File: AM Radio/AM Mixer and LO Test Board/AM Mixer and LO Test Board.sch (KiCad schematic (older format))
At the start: 53 parts, among them J1 RF_IN, J2 IF_FILT_OUT, J3 IF_PREFILT_OUT, J4 RF_IN, J5 +12V Input, J6 -12V Input, Q1 2N2222, Q2 2N2222, Q3 2N2222, T1 SWB2010-1-SM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

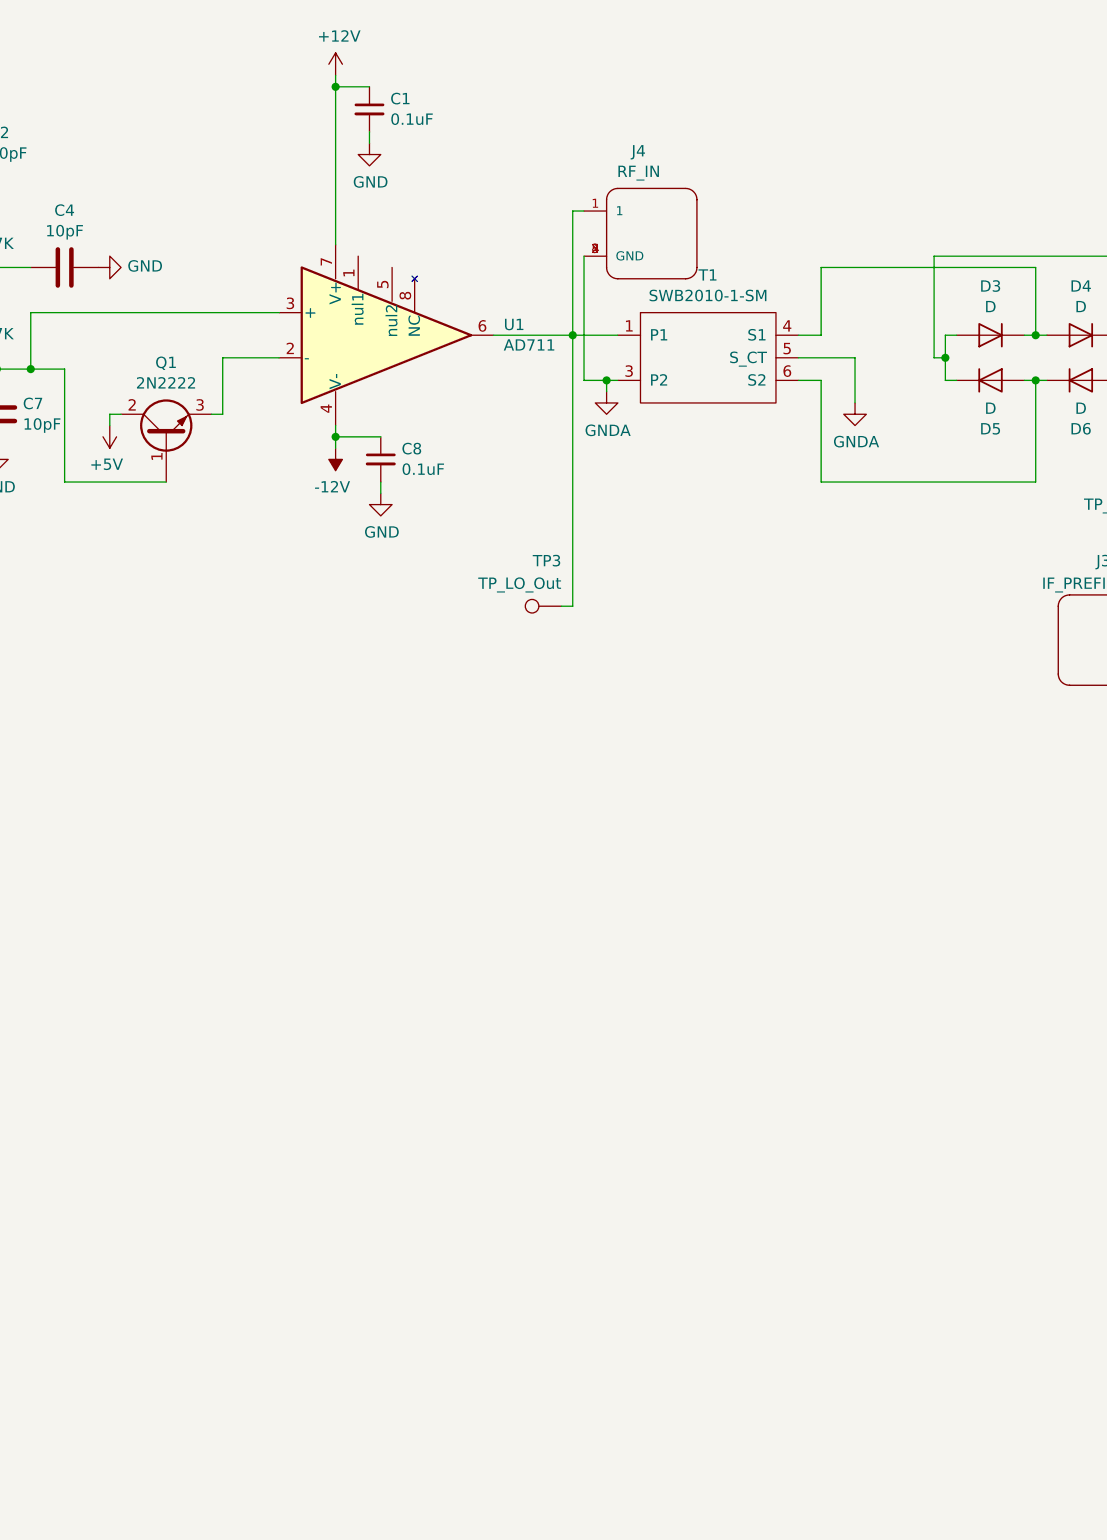
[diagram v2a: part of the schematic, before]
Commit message: Added extra filter for testing. Finished silk screen editing.
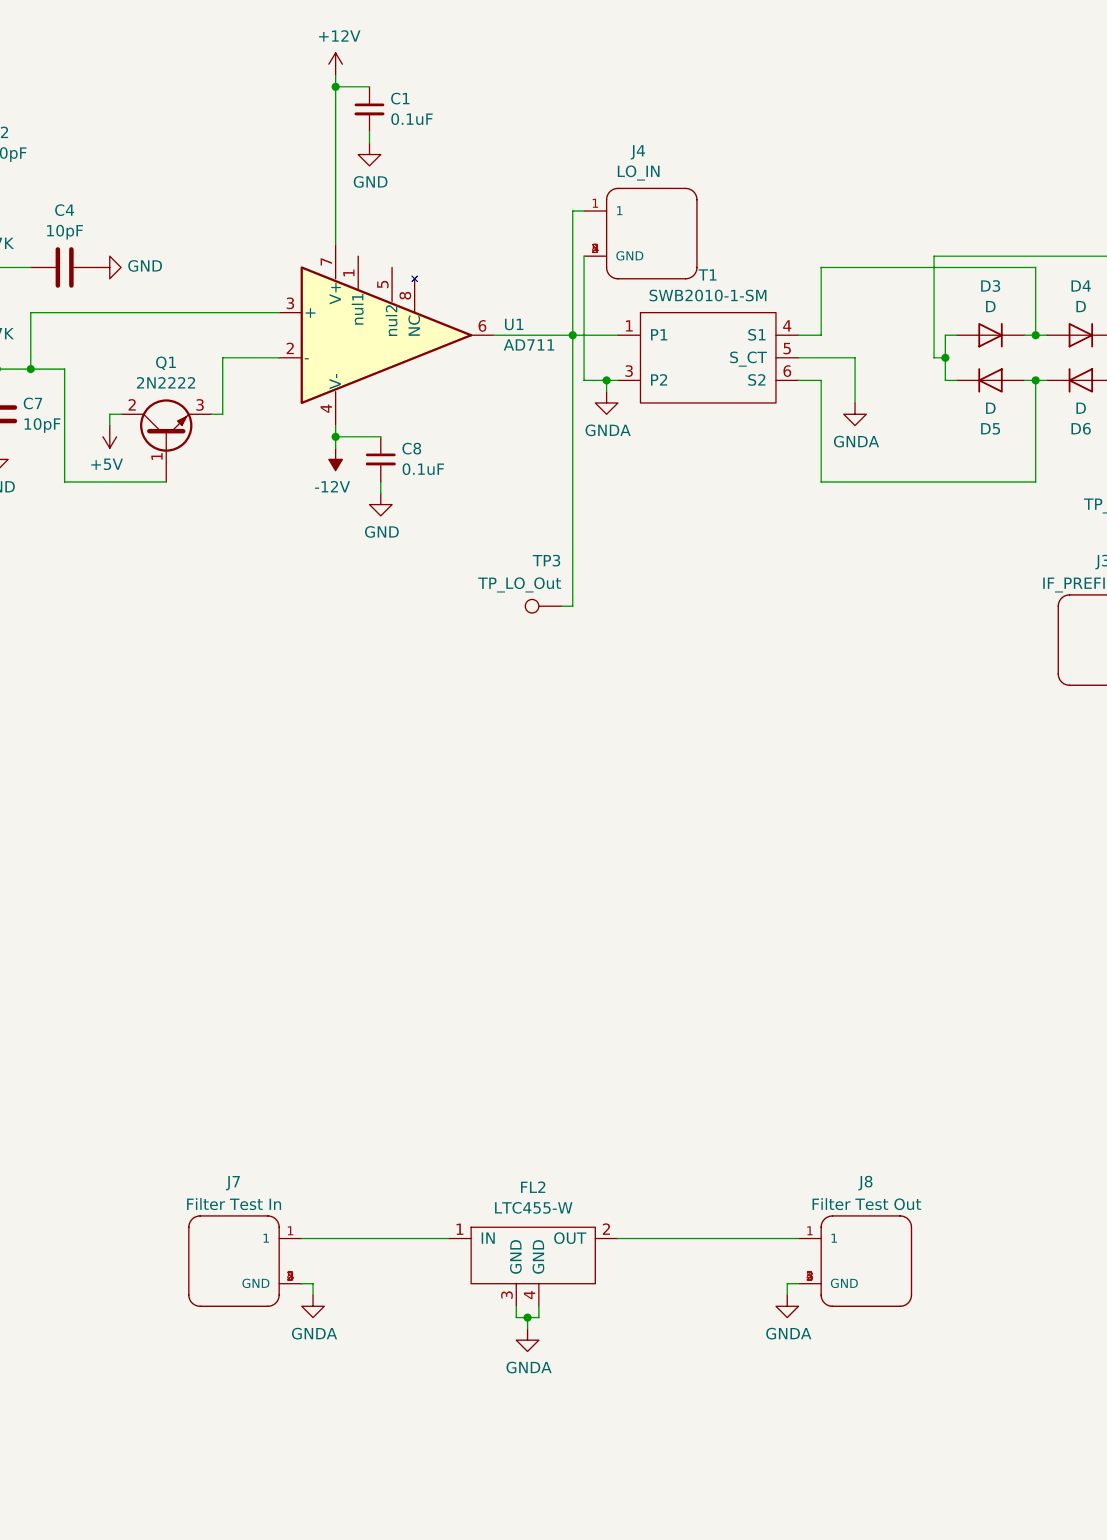
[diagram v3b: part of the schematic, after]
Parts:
- added FL2: LTC455-W, footprints:LTC455-W, symbol CustomComponents:LTC455-W
- added J7: Filter Test In, footprints:TE_5-1634503-1, symbol TE_5-1634503-1:5-1634503-1
- added J8: Filter Test Out, footprints:TE_5-1634503-1, symbol TE_5-1634503-1:5-1634503-1
- J4: value RF_IN -> LO_IN
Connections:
- net GNDA: now also FL2.3 (GND), FL2.4 (GND), J7.2 (GND), J7.3 (GND), J7.4 (GND), J7.5 (GND), J8.2 (GND), J8.3 (GND), J8.4 (GND), J8.5 (GND)
- new net: FL2.2 (OUT), J8.1
- new net: FL2.1 (IN), J7.1
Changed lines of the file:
@@
 P 9900 2750
 F 0 "J4" H 9958 3115 50  0000 C CNN
-F 1 "RF_IN" H 9958 3024 50  0000 C CNN
+F 1 "LO_IN" H 9958 3024 50  0000 C CNN
 F 2 "footprints:TE_5-1634503-1" H 9900 2750 50  0001 L BNN
 F 3 "" H 9900 2750 50  0001 L BNN
@@
 Wire Wire Line
 	4550 1500 4550 1400
+$Comp
+L TE_5-1634503-1:5-1634503-1 J8
+U 1 1 60DEE717
+P 10850 7300
+F 0 "J8" H 10850 7650 50  0000 C CNN
+F 1 "Filter Test Out" H 10850 7550 50  0000 C CNN
+F 2 "footprints:TE_5-1634503-1" H 10850 7300 50  0001 L BNN
+F 3 "" H 10850 7300 50  0001 L BNN
+F 4 "1" H 10850 7300 50  0001 L BNN "Number_of_Positions"
+F 5 "Compliant" H 10850 7300 50  0001 L BNN "EU_RoHS_Compliance"
+F 6 "5-1634503-1" H 10850 7300 50  0001 L BNN "Comment"
+	1    10850 7300
+	-1   0    0    -1
+$EndComp
+$Comp
+L power:GNDA #PWR043
+U 1 1 60DEE71D
+P 10500 7450
+F 0 "#PWR043" H 10500 7200 50  0001 C CNN
+F 1 "GNDA" H 10505 7277 50  0000 C CNN
+F 2 "" H 10500 7450 50  0001 C CNN
+F 3 "" H 10500 7450 50  0001 C CNN
+	1    10500 7450
+	1    0    0    -1
+$EndComp
+Wire Wire Line
+	10500 7450 10500 7400
+Wire Wire Line
+	10500 7400 10550 7400
+$Comp
+L TE_5-1634503-1:5-1634503-1 J7
+U 1 1 60DEE728
+P 8050 7300
+F 0 "J7" H 8050 7650 50  0000 C CNN
+F 1 "Filter Test In" H 8050 7550 50  0000 C CNN
+F 2 "footprints:TE_5-1634503-1" H 8050 7300 50  0001 L BNN
+F 3 "" H 8050 7300 50  0001 L BNN
+F 4 "1" H 8050 7300 50  0001 L BNN "Number_of_Positions"
+F 5 "Compliant" H 8050 7300 50  0001 L BNN "EU_RoHS_Compliance"
+F 6 "5-1634503-1" H 8050 7300 50  0001 L BNN "Comment"
+	1    8050 7300
+	1    0    0    -1
+$EndComp
+$Comp
+L CustomComponents:LTC455-W FL2
+U 1 1 60DEE72E
+P 9350 7400
+F 0 "FL2" H 9375 7825 50  0000 C CNN
+F 1 "LTC455-W" H 9375 7734 50  0000 C CNN
+F 2 "footprints:LTC455-W" H 9100 7700 50  0001 C CNN
+F 3 "" H 9100 7700 50  0001 C CNN
+	1    9350 7400
+	1    0    0    -1
+$EndComp
+$Comp
+L power:GNDA #PWR044
+U 1 1 60DEE734
+P 9350 7600
+F 0 "#PWR044" H 9350 7350 50  0001 C CNN
+F 1 "GNDA" H 9355 7427 50  0000 C CNN
+F 2 "" H 9350 7600 50  0001 C CNN
+F 3 "" H 9350 7600 50  0001 C CNN
+	1    9350 7600
+	1    0    0    -1
+$EndComp
+Wire Wire Line
+	9350 7600 9350 7550
+Wire Wire Line
+	9350 7550 9300 7550
+Wire Wire Line
+	9300 7550 9300 7500
+Wire Wire Line
+	9350 7550 9400 7550
+Wire Wire Line
+	9400 7550 9400 7500
+Connection ~ 9350 7550
+Wire Wire Line
+	9750 7200 10550 7200
+$Comp
+L power:GNDA #PWR042
+U 1 1 60DEE746
+P 8400 7450
+F 0 "#PWR042" H 8400 7200 50  0001 C CNN
+F 1 "GNDA" H 8405 7277 50  0000 C CNN
+F 2 "" H 8400 7450 50  0001 C CNN
+F 3 "" H 8400 7450 50  0001 C CNN
+	1    8400 7450
+	1    0    0    -1
+$EndComp
+Wire Wire Line
+	8400 7450 8400 7400
+Wire Wire Line
+	8400 7400 8350 7400
+Wire Wire Line
+	8350 7200 9000 7200
 $EndSCHEMATC
